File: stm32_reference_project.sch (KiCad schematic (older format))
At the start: 42 parts, among them J1 USB_Serial, J2 PROG_HDR, SW1 RESET, SW2 BAT_SELECT, SW3 BOOT_SELECT, U1 MIC5501-3.0YM5, U2 STM32F103C8Tx, Y1 8Mhz, Y2 32.768K

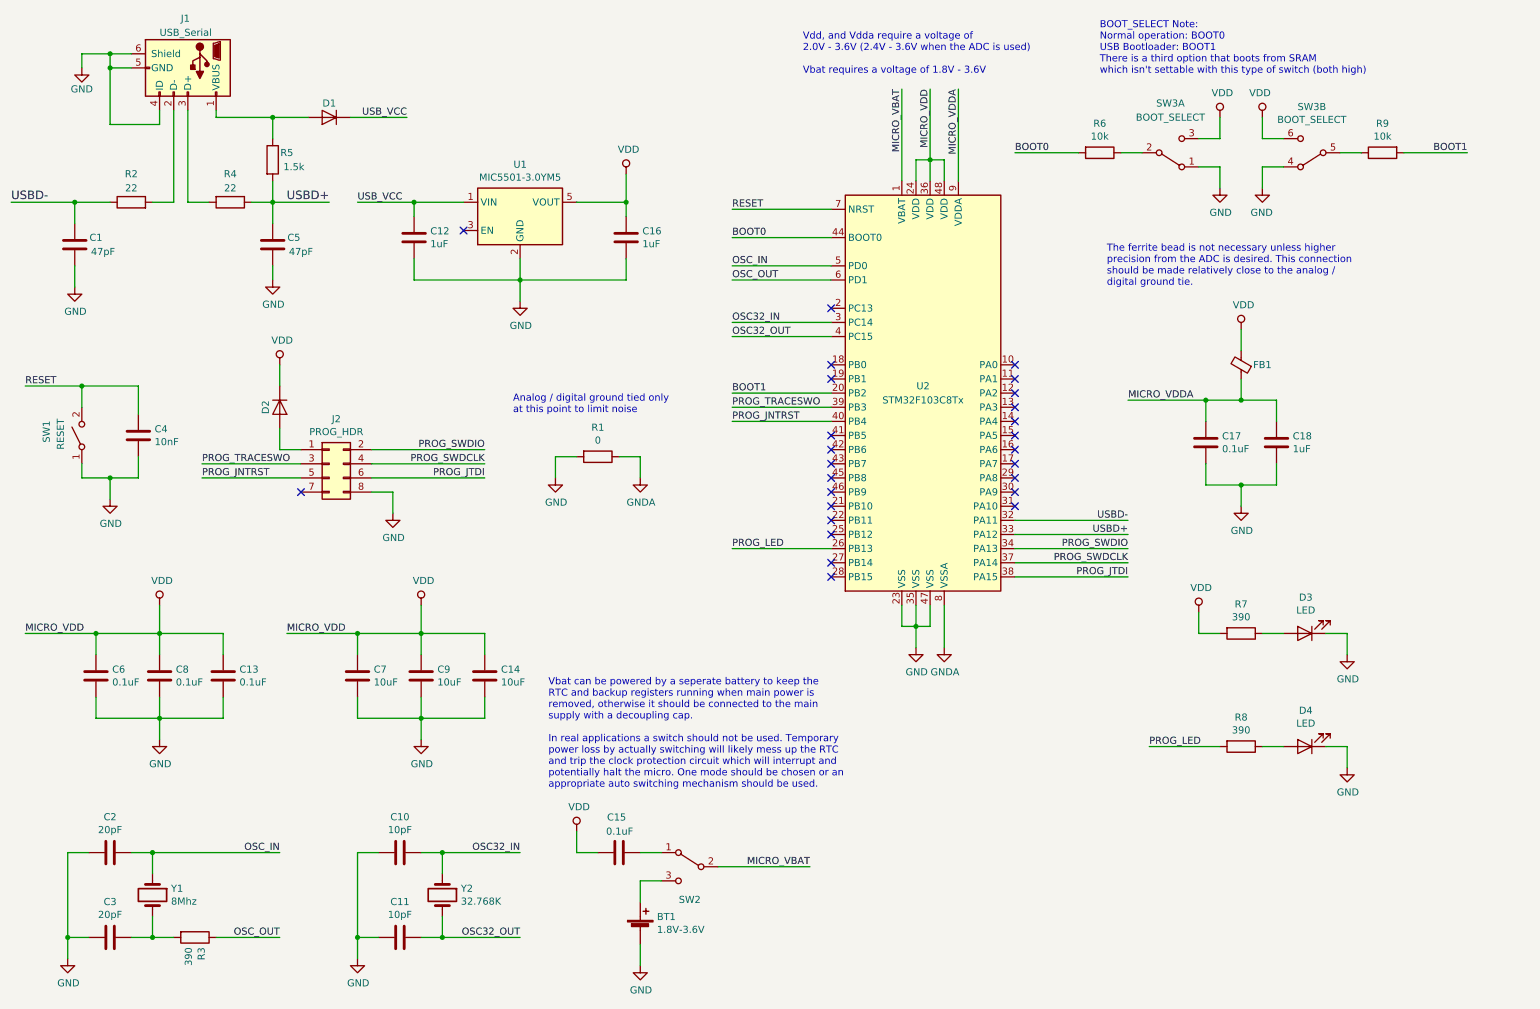
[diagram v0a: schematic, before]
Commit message: Was using a bad linear regulator
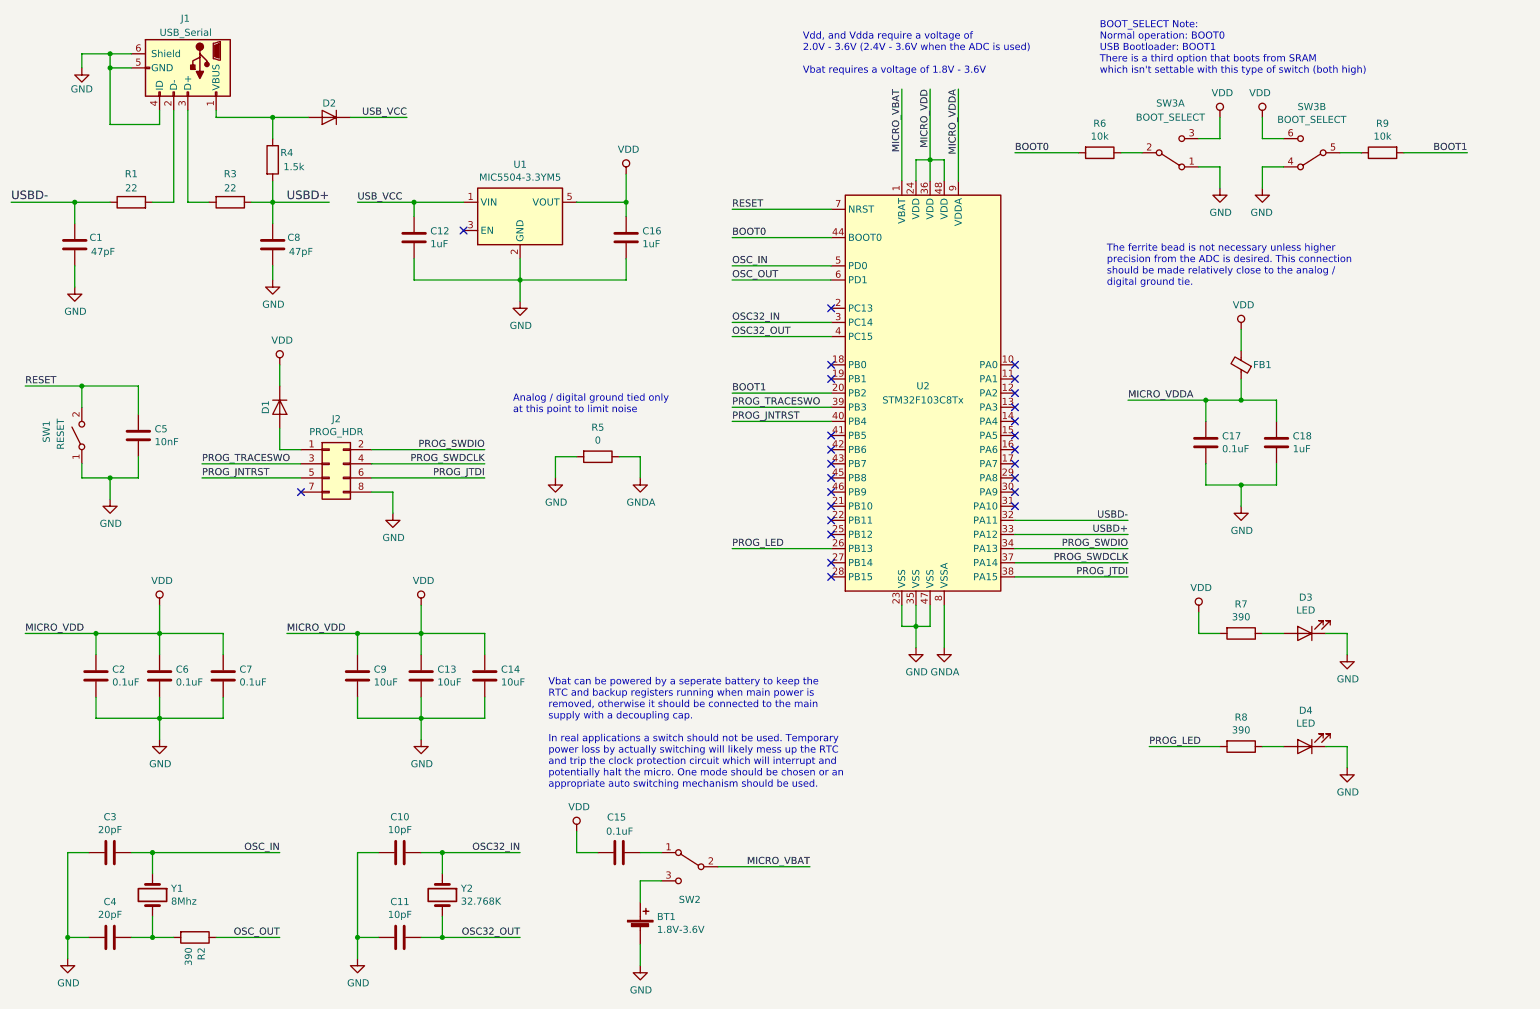
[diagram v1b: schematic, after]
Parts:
- removed U1: MIC5501-3.0YM5, Package_TO_SOT_SMD:SOT-23-5, symbol Regulator_Linear:MIC5501-3.0YM5
- added U1: MIC5504-3.3YM5, Package_TO_SOT_SMD:SOT-23-5, symbol Regulator_Linear:MIC5504-3.3YM5
- renumbered C9 to C13, C6 to C2, C2 to C3, C3 to C4, C4 to C5, C8 to C6, C13 to C7, C5 to C8, C7 to C9, D2 to D1, D1 to D2, R2 to R1, R3 to R2, R4 to R3, R5 to R4, R1 to R5
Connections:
- net GND: now also U1.2 (GND)
- net USB_VCC: now also U1.1 (VIN)
- net VDD: now also U1.5 (VOUT)
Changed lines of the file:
@@
 $EndDescr
 $Comp
-L Device:C C6
+L Device:C C2
 U 1 1 5C54792D
 P 1200 5250
-F 0 "C6" H 1315 5296 50  0000 L CNN
+F 0 "C2" H 1315 5296 50  0000 L CNN
 F 1 "0.1uF" H 1315 5205 50  0000 L CNN
 F 2 "Capacitor_SMD:C_0603_1608Metric" H 1238 5100 50  0001 C CNN
@@
 $EndComp
 $Comp
-L Device:C C8
+L Device:C C6
 U 1 1 5C548A3E
 P 1650 5250
-F 0 "C8" H 1765 5296 50  0000 L CNN
+F 0 "C6" H 1765 5296 50  0000 L CNN
 F 1 "0.1uF" H 1765 5205 50  0000 L CNN
 F 2 "Capacitor_SMD:C_0603_1608Metric" H 1688 5100 50  0001 C CNN
@@
 $EndComp
 $Comp
-L Device:C C13
+L Device:C C7
 U 1 1 5C548CA4
 P 2100 5250
-F 0 "C13" H 2215 5296 50  0000 L CNN
+F 0 "C7" H 2215 5296 50  0000 L CNN
 F 1 "0.1uF" H 2215 5205 50  0000 L CNN
 F 2 "Capacitor_SMD:C_0603_1608Metric" H 2138 5100 50  0001 C CNN
@@
 Connection ~ 1650 4950
 $Comp
-L power:GND #PWR010
+L power:GND #PWR06
 U 1 1 5C54ED17
 P 1650 5700
-F 0 "#PWR010" H 1650 5450 50  0001 C CNN
+F 0 "#PWR06" H 1650 5450 50  0001 C CNN
 F 1 "GND" H 1655 5527 50  0000 C CNN
 F 2 "" H 1650 5700 50  0001 C CNN
@@
 $EndComp
 $Comp
-L power:GND #PWR04
+L power:GND #PWR03
 U 1 1 5A74F566
 P 1100 950
-F 0 "#PWR04" H 1100 700 50  0001 C CNN
+F 0 "#PWR03" H 1100 700 50  0001 C CNN
 F 1 "GND" H 1100 800 50  0000 C CNN
 F 2 "" H 1100 950 50  0001 C CNN
@@
 	1450 950  1300 950
 $Comp
-L stm32_reference_project-rescue:R-relay_system_controller-rescue-relay_system_controller-rescue R4
+L stm32_reference_project-rescue:R-relay_system_controller-rescue-relay_system_controller-rescue R3
 U 1 1 5ADA1249
 P 2150 1900
-F 0 "R4" V 1950 1900 50  0000 C CNN
+F 0 "R3" V 1950 1900 50  0000 C CNN
 F 1 "22" V 2050 1900 50  0000 C CNN
 F 2 "Resistor_SMD:R_0603_1608Metric" V 2080 1900 50  0001 C CNN
@@
 $EndComp
 $Comp
-L stm32_reference_project-rescue:R-relay_system_controller-rescue-relay_system_controller-rescue R5
+L stm32_reference_project-rescue:R-relay_system_controller-rescue-relay_system_controller-rescue R4
 U 1 1 5ADA14FC
 P 2450 1600
-F 0 "R5" H 2550 1650 50  0000 C CNN
+F 0 "R4" H 2550 1650 50  0000 C CNN
 F 1 "1.5k" H 2600 1550 50  0000 C CNN
 F 2 "Resistor_SMD:R_0603_1608Metric" V 2380 1600 50  0001 C CNN
@@
 $EndComp
 $Comp
-L stm32_reference_project-rescue:R-relay_system_controller-rescue-relay_system_controller-rescue R2
+L stm32_reference_project-rescue:R-relay_system_controller-rescue-relay_system_controller-rescue R1
 U 1 1 5ADA17B2
 P 1450 1900
-F 0 "R2" V 1650 1900 50  0000 C CNN
+F 0 "R1" V 1650 1900 50  0000 C CNN
 F 1 "22" V 1550 1900 50  0000 C CNN
 F 2 "Resistor_SMD:R_0603_1608Metric" V 1380 1900 50  0001 C CNN
@@
 $EndComp
 $Comp
-L Device:C C5
+L Device:C C8
 U 1 1 5C0BA9F9
 P 2450 2200
-F 0 "C5" H 2300 2150 50  0000 C CNN
+F 0 "C8" H 2300 2150 50  0000 C CNN
 F 1 "47pF" H 2250 2250 50  0000 C CNN
 F 2 "Capacitor_SMD:C_0603_1608Metric" H 2488 2050 50  0001 C CNN
@@
 $EndComp
 $Comp
-L power:GND #PWR03
+L power:GND #PWR02
 U 1 1 5C0BD417
 P 1050 2500
-F 0 "#PWR03" H 1050 2250 50  0001 C CNN
+F 0 "#PWR02" H 1050 2250 50  0001 C CNN
 F 1 "GND" H 1055 2327 50  0000 C CNN
 F 2 "" H 1050 2500 50  0001 C CNN
@@
 $EndComp
 $Comp
-L power:GND #PWR02
+L power:GND #PWR01
 U 1 1 5C112DF0
 P 1000 7250
-F 0 "#PWR02" H 1000 7000 50  0001 C CNN
+F 0 "#PWR01" H 1000 7000 50  0001 C CNN
 F 1 "GND" H 1005 7077 50  0000 C CNN
 F 2 "" H 1000 7250 50  0001 C CNN
@@
 $EndComp
 $Comp
-L Device:C C3
+L Device:C C4
 U 1 1 5C1161FC
 P 1300 7100
-F 0 "C3" V 1048 7100 50  0000 C CNN
+F 0 "C4" V 1048 7100 50  0000 C CNN
 F 1 "20pF" V 1139 7100 50  0000 C CNN
 F 2 "Capacitor_SMD:C_0603_1608Metric" H 1338 6950 50  0001 C CNN
@@
 $EndComp
 $Comp
-L Device:C C2
+L Device:C C3
 U 1 1 5C1174FD
 P 1300 6500
-F 0 "C2" V 1048 6500 50  0000 C CNN
+F 0 "C3" V 1048 6500 50  0000 C CNN
 F 1 "20pF" V 1139 6500 50  0000 C CNN
 F 2 "Capacitor_SMD:C_0603_1608Metric" H 1338 6350 50  0001 C CNN
@@
 $EndComp
 $Comp
-L power:GND #PWR08
+L power:GND #PWR09
 U 1 1 5C33BFCF
 P 3050 7250
-F 0 "#PWR08" H 3050 7000 50  0001 C CNN
+F 0 "#PWR09" H 3050 7000 50  0001 C CNN
 F 1 "GND" H 3055 7077 50  0000 C CNN
 F 2 "" H 3050 7250 50  0001 C CNN
@@
 $EndComp
 $Comp
-L power:GND #PWR05
+L power:GND #PWR04
 U 1 1 5C1944A1
 P 1300 4000
-AR Path="/5C1944A1" Ref="#PWR05"  Part="1"
+AR Path="/5C1944A1" Ref="#PWR04"  Part="1"
 AR Path="/5C77D6A4/5C1944A1" Ref="#PWR?"  Part="1"
-F 0 "#PWR05" H 1300 3750 50  0001 C CNN
+F 0 "#PWR04" H 1300 3750 50  0001 C CNN
 F 1 "GND" H 1305 3827 50  0000 C CNN
 F 2 "" H 1300 4000 50  0001 C CNN
@@
 	700  3200 1100 3200
 $Comp
-L Device:R R3
+L Device:R R2
 U 1 1 5C5787B0
 P 1900 7100
-F 0 "R3" H 1970 7146 50  0000 L CNN
+F 0 "R2" H 1970 7146 50  0000 L CNN
 F 1 "390" H 1970 7055 50  0000 L CNN
 F 2 "Resistor_SMD:R_0603_1608Metric" V 1830 7100 50  0001 C CNN
@@
 Connection ~ 1200 4950
 $Comp
-L power:GND #PWR01
+L power:GND #PWR014
 U 1 1 5C7B2CA7
 P 4450 3850
-F 0 "#PWR01" H 4450 3600 50  0001 C CNN
+F 0 "#PWR014" H 4450 3600 50  0001 C CNN
 F 1 "GND" H 4455 3677 50  0000 C CNN
 F 2 "" H 4450 3850 50  0001 C CNN
@@
 $EndComp
 $Comp
-L power:GNDA #PWR06
+L power:GNDA #PWR017
 U 1 1 5C7B330D
 P 5050 3850
-F 0 "#PWR06" H 5050 3600 50  0001 C CNN
+F 0 "#PWR017" H 5050 3600 50  0001 C CNN
 F 1 "GNDA" H 5055 3677 50  0000 C CNN
 F 2 "" H 5050 3850 50  0001 C CNN
@@
 $EndComp
 $Comp
-L Device:R R1
+L Device:R R5
 U 1 1 5C7B39AF
 P 4750 3700
-F 0 "R1" V 4543 3700 50  0000 C CNN
+F 0 "R5" V 4543 3700 50  0000 C CNN
 F 1 "0" V 4634 3700 50  0000 C CNN
 F 2 "Resistor_SMD:R_0402_1005Metric" V 4680 3700 50  0001 C CNN
@@
 	4450 3700 4450 3850
 $Comp
-L power:GND #PWR017
+L power:GND #PWR018
 U 1 1 5C7EE652
 P 5050 7300
-F 0 "#PWR017" H 5050 7050 50  0001 C CNN
+F 0 "#PWR018" H 5050 7050 50  0001 C CNN
 F 1 "GND" H 5055 7127 50  0000 C CNN
 F 2 "" H 5050 7300 50  0001 C CNN
@@
 	9300 3300 9550 3300
 $Comp
-L power:VDD #PWR09
+L power:VDD #PWR05
 U 1 1 5C89E838
 P 1650 4750
-F 0 "#PWR09" H 1650 4600 50  0001 C CNN
+F 0 "#PWR05" H 1650 4600 50  0001 C CNN
 F 1 "VDD" H 1667 4923 50  0000 C CNN
 F 2 "" H 1650 4750 50  0001 C CNN
@@
 $EndComp
 $Comp
-L Device:C C4
+L Device:C C5
 U 1 1 5C566DDD
 P 1500 3550
-F 0 "C4" H 1615 3596 50  0000 L CNN
+F 0 "C5" H 1615 3596 50  0000 L CNN
 F 1 "10nF" H 1615 3505 50  0000 L CNN
 F 2 "" H 1538 3400 50  0001 C CNN
@@
 Connection ~ 1100 3200
 $Comp
-L power:VDD #PWR014
+L power:VDD #PWR015
 U 1 1 5C91AD3F
 P 4600 6350
-F 0 "#PWR014" H 4600 6200 50  0001 C CNN
+F 0 "#PWR015" H 4600 6200 50  0001 C CNN
 F 1 "VDD" H 4617 6523 50  0000 C CNN
 F 2 "" H 4600 6350 50  0001 C CNN
@@
 	1    0    0    -1
 $EndComp
-$Comp
-L Regulator_Linear:MIC5501-3.0YM5 U1
-U 1 1 5C5B51DF
-P 4200 2000
-F 0 "U1" H 4200 2367 50  0000 C CNN
-F 1 "MIC5501-3.0YM5" H 4200 2276 50  0000 C CNN
-F 2 "Package_TO_SOT_SMD:SOT-23-5" H 4200 1600 50  0001 C CNN
-F 3 "http://ww1.microchip.com/downloads/en/DeviceDoc/MIC550X.pdf" H 3950 2250 50  0001 C CNN
-	1    4200 2000
-	1    0    0    -1
-$EndComp
 Text Notes 4400 6050 0    50   ~ 0
 Vbat can be powered by a seperate battery to keep the\nRTC and backup registers running when main power is\nremoved, otherwise it should be connected to the main\nsupply with a decoupling cap.\n\nIn real applications a switch should not be used. Temporary\npower loss by actually switching will likely mess up the RTC\nand trip the clock protection circuit which will interrupt and\npotentially halt the micro. One mode should be chosen or an\nappropriate auto switching mechanism should be used.
@@
 $EndComp
 $Comp
-L Device:C C7
+L Device:C C9
 U 1 1 5C7AE177
 P 3050 5250
-F 0 "C7" H 3165 5296 50  0000 L CNN
+F 0 "C9" H 3165 5296 50  0000 L CNN
 F 1 "10uF" H 3165 5205 50  0000 L CNN
 F 2 "Capacitor_SMD:C_0603_1608Metric" H 3088 5100 50  0001 C CNN
@@
 	2500 3050 2500 3200
 $Comp
-L Device:D D2
+L Device:D D1
 U 1 1 5CA5FD4B
 P 2500 3350
-AR Path="/5CA5FD4B" Ref="D2"  Part="1"
+AR Path="/5CA5FD4B" Ref="D1"  Part="1"
 AR Path="/5C277487/5CA5FD4B" Ref="D?"  Part="1"
-F 0 "D2" H 2500 3250 50  0000 C CNN
+F 0 "D1" H 2500 3250 50  0000 C CNN
 F 1 "NEEDS_SPEC" H 2500 3225 50  0001 C CNN
 F 2 "Diode_SMD:D_SOD-123" H 2500 3350 50  0001 C CNN
@@
 	3300 4100 3300 3950
 $Comp
-L power:GND #PWR018
+L power:GND #PWR010
 U 1 1 5C901C3E
 P 3300 4100
-F 0 "#PWR018" H 3300 3850 50  0001 C CNN
+F 0 "#PWR010" H 3300 3850 50  0001 C CNN
 F 1 "GND" H 3305 3927 50  0000 C CNN
 F 2 "" H 3300 4100 50  0001 C CNN
@@
 	2500 3500 2500 3650
 $Comp
-L power:VDD #PWR015
+L power:VDD #PWR08
 U 1 1 5C8FA548
 P 2500 3050
-F 0 "#PWR015" H 2500 2900 50  0001 C CNN
+F 0 "#PWR08" H 2500 2900 50  0001 C CNN
 F 1 "VDD" H 2517 3223 50  0000 C CNN
 F 2 "" H 2500 3050 50  0001 C CNN
@@
 PROG_TRACESWO
 $Comp
-L Device:D D1
+L Device:D D2
 U 1 1 5C0D38F7
 P 2850 1300
-AR Path="/5C0D38F7" Ref="D1"  Part="1"
+AR Path="/5C0D38F7" Ref="D2"  Part="1"
 AR Path="/5C277487/5C0D38F7" Ref="D?"  Part="1"
-F 0 "D1" H 2850 1200 50  0000 C CNN
+F 0 "D2" H 2850 1200 50  0000 C CNN
 F 1 "NEEDS_SPEC" H 2850 1175 50  0001 C CNN
 F 2 "Diode_SMD:D_SOD-123" H 2850 1300 50  0001 C CNN
@@
 $EndComp
 $Comp
-L Device:C C9
+L Device:C C13
 U 1 1 5C7AE180
 P 3500 5250
-F 0 "C9" H 3615 5296 50  0000 L CNN
+F 0 "C13" H 3615 5296 50  0000 L CNN
 F 1 "10uF" H 3615 5205 50  0000 L CNN
 F 2 "Capacitor_SMD:C_0603_1608Metric" H 3538 5100 50  0001 C CNN
@@
 Text Notes 4150 3400 0    50   ~ 0
 Analog / digital ground tied only\nat this point to limit noise
+$Comp
+L Regulator_Linear:MIC5504-3.3YM5 U1
+U 1 1 5D05898C
+P 4200 2000
+F 0 "U1" H 4200 2367 50  0000 C CNN
+F 1 "MIC5504-3.3YM5" H 4200 2276 50  0000 C CNN
+F 2 "Package_TO_SOT_SMD:SOT-23-5" H 4200 1600 50  0001 C CNN
+F 3 "http://ww1.microchip.com/downloads/en/DeviceDoc/MIC550X.pdf" H 3950 2250 50  0001 C CNN
+	1    4200 2000
+	1    0    0    -1
+$EndComp
 $EndSCHEMATC

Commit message: More refinements on the reference project
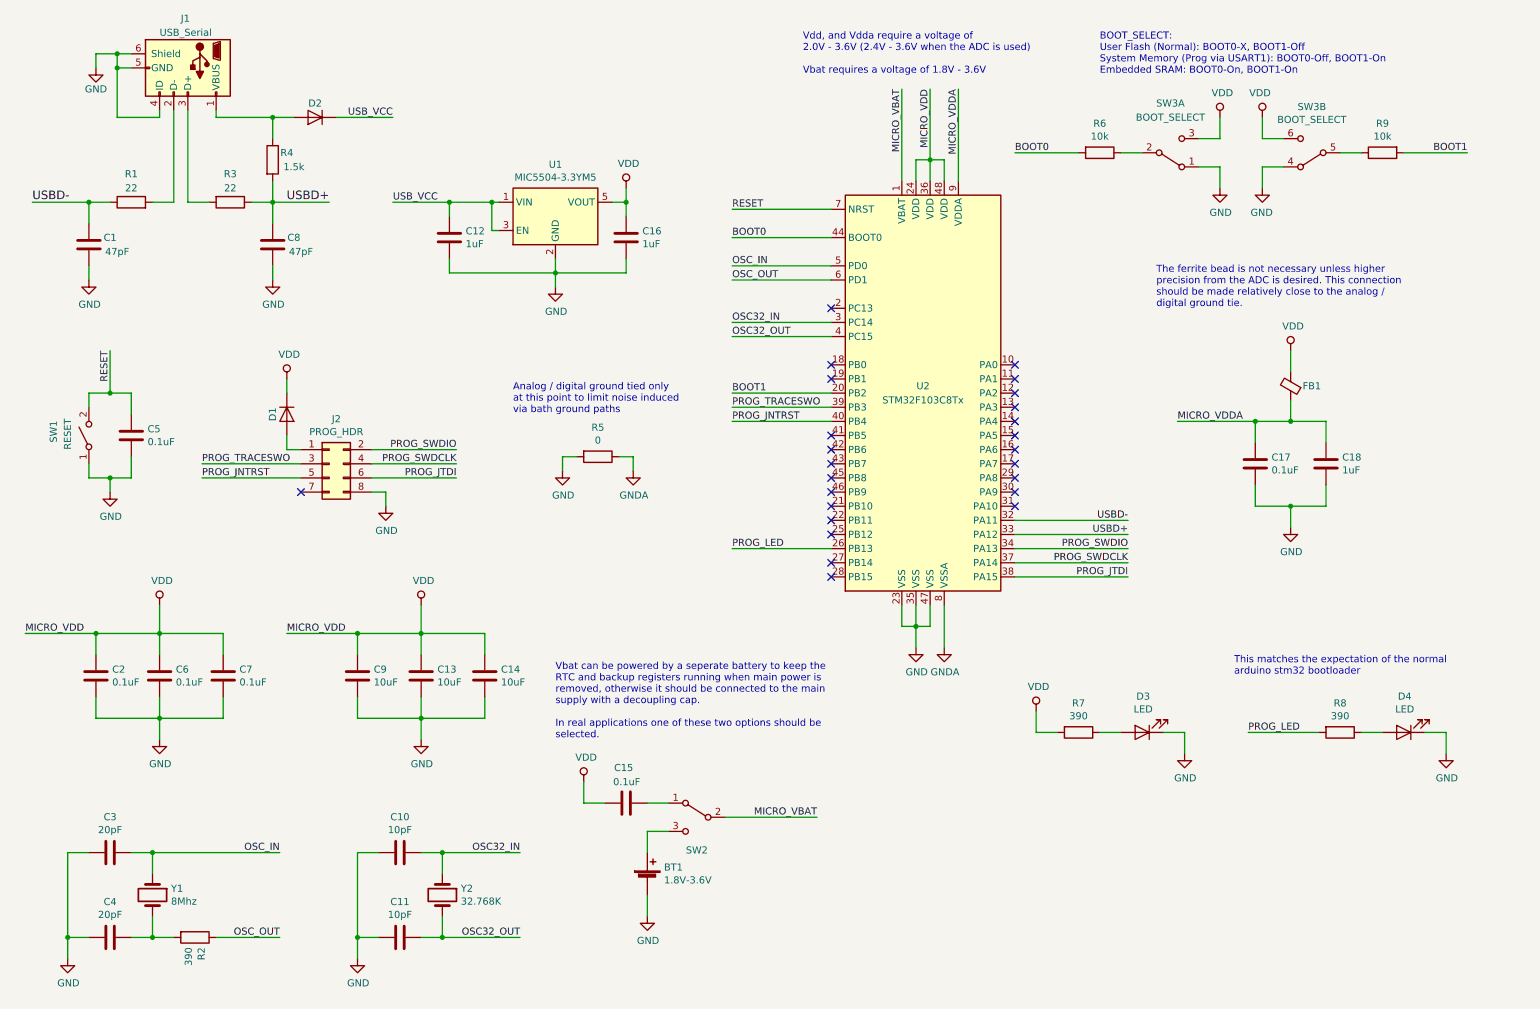
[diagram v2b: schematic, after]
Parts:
- C5: value 10nF -> 0.1uF; footprint (none) -> Capacitor_SMD:C_0603_1608Metric; Spice_Model 100nF -> 100n
- D3, D4: footprint (none) -> Diode_SMD:D_SOD-123
- R7, R8: footprint (none) -> Resistor_SMD:R_0603_1608Metric; Spice_Model (none) -> 390; Spice_Netlist_Enabled (none) -> Y; Spice_Primitive (none) -> R
- SW3: footprint Button_Switch_THT:SW_E-Switch_EG1271_DPDT -> Button_Switch_THT:SW_DIP_SPSTx02_Slide_9.78x7.26mm_W7.62mm_P2.54mm; DigiKey Part (none) -> CT2102MS-ND; DigiKey Price (none) -> 0.43
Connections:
- net USB_VCC: now also U1.3 (EN)
- no-connect marks 26 -> 25
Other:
- note added: "Analog / digital ground tied only\nat this point to limit noise induced\nvia bath ground paths"
- note added: "BOOT_SELECT:\nUser Flash (Normal): BOOT0-X, BOOT1-Off\nSystem Memory (Prog via USART1): BOOT0-Off, BOOT1-On\nEmbedded SRAM: BOOT0-On, BOOT1-On"
- note added: "This matches the expectation of the normal\narduino stm32 bootloader"
- note added: "Vbat can be powered by a seperate battery to keep the\nRTC and backup registers running when main power is\nremoved, otherwise it should be connected to the main\nsupply with a decoupling cap.\n\nIn real applications one of these two options should be\nselected."
- note removed: "Analog / digital ground tied only\nat this point to limit noise"
- note removed: "BOOT_SELECT Note:\nNormal operation: BOOT0\nUSB Bootloader: BOOT1\nThere is a third option that boots from SRAM\nwhich isn't settable with this type of switch (both high)"
- note removed: "Vbat can be powered by a seperate battery to keep the\nRTC and backup registers running when main power is\nremoved, otherwise it should be connected to the main\nsupply with a decoupling cap.\n\nIn real applications a switch should not be used. Temporary\npower loss by actually switching will likely mess up the RTC\nand trip the clock protection circuit which will interrupt and\npotentially halt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"
- moved on the sheet: BT1, C1, C12, C15, C17, C18, C5, D1, D2, D3, D4, FB1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
